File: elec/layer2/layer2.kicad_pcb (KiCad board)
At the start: 2 copper layers, 178 x 173.3 mm, 33 parts, among them J1 Conn_01x08, J2 Conn_01x08, J3 Conn_01x08, J4 Conn_01x08

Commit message: l1 half motors done
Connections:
- L1-->l2Connection1 pad 1: /Dribbler Data -> /LightGateLDR
- L1-->l2Connection1 pad 2: /LightGateLDR -> /Dribbler Data
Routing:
- net /Dribbler Data: track 108.4 -> 112.0 mm
- net /LightGateLDR: track 122.2 -> 123.5 mm
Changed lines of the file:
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@@
 			(layers "*.Cu" "*.Mask")
 			(remove_unused_layers no)
-			(net 15 "/Dribbler Data")
+			(net 2 "/LightGateLDR")
 			(pinfunction "Pin_1")
 			(pintype "passive")
@@
 			(layers "*.Cu" "*.Mask")
 			(remove_unused_layers no)
-			(net 2 "/LightGateLDR")
+			(net 15 "/Dribbler Data")
 			(pinfunction "Pin_2")
 			(pintype "passive")
@@
 	)
 	(segment
+		(start 91.407681 47.345234)
+		(end 93.607681 47.345234)
+		(width 0.2)
+		(layer "F.Cu")
+		(net 2)
+	)
+	(segment
 		(start 89.557681 144.245234)
 		(end 89.557681 157.995234)
@@
 	)
 	(segment
-		(start 88.707681 45.845234)
-		(end 89.747681 44.805234)
+		(start 91.207681 105.495234)
+		(end 91.207681 106.445234)
+		(width 0.2)
+		(layer "F.Cu")
+		(net 2)
+	)
+	(segment
+		(start 93.407681 106.845234)
+		(end 94.107681 106.145234)
 		(width 0.2)
 		(layer "F.Cu")
@@
 	)
 	(segment
-		(start 88.707681 102.545234)
-		(end 88.707681 45.845234)
+		(start 90.307681 99.745234)
+		(end 90.307681 48.445234)
 		(width 0.2)
 		(layer "F.Cu")
@@
 	)
 	(segment
-		(start 91.207681 105.045234)
-		(end 88.707681 102.545234)
+		(start 91.607681 106.845234)
+		(end 93.407681 106.845234)
 		(width 0.2)
 		(layer "F.Cu")
@@
 	)
 	(segment
-		(start 91.207681 127.745234)
-		(end 91.207681 142.595234)
+		(start 91.207681 106.445234)
+		(end 91.607681 106.845234)
 		(width 0.2)
 		(layer "F.Cu")
@@
 	)
 	(segment
-		(start 89.747681 44.805234)
-		(end 93.607681 44.805234)
+		(start 94.107681 103.545234)
+		(end 90.307681 99.745234)
 		(width 0.2)
 		(layer "F.Cu")
@@
 	)
 	(segment
-		(start 91.207681 105.495234)
-		(end 91.207681 105.045234)
+		(start 94.107681 106.145234)
+		(end 94.107681 103.545234)
+		(width 0.2)
+		(layer "F.Cu")
+		(net 2)
+	)
+	(segment
+		(start 90.307681 48.445234)
+		(end 91.407681 47.345234)
+		(width 0.2)
+		(layer "F.Cu")
+		(net 2)
+	)
+	(segment
+		(start 91.207681 127.745234)
+		(end 91.207681 142.595234)
 		(width 0.2)
 		(layer "F.Cu")
@@
 	)
 	(segment
-		(start 90.407681 101.945234)
-		(end 92.907681 104.445234)
+		(start 88.707681 47.545234)
+		(end 91.447681 44.805234)
 		(width 0.2)
 		(layer "F.Cu")
@@
 	(segment
 		(start 92.907681 104.445234)
-		(end 92.907681 105.445234)
+		(end 88.707681 100.245234)
 		(width 0.2)
 		(layer "F.Cu")
@@
 	)
 	(segment
-		(start 90.807681 47.345234)
-		(end 90.407681 47.745234)
+		(start 92.907681 105.445234)
+		(end 92.907681 104.445234)
 		(width 0.2)
 		(layer "F.Cu")
@@
 	)
 	(segment
-		(start 90.407681 47.745234)
-		(end 90.407681 101.945234)
+		(start 91.447681 44.805234)
+		(end 93.607681 44.805234)
 		(width 0.2)
 		(layer "F.Cu")
@@
 	)
 	(segment
-		(start 93.607681 47.345234)
-		(end 90.807681 47.345234)
+		(start 88.707681 100.245234)
+		(end 88.707681 47.545234)
 		(width 0.2)
 		(layer "F.Cu")

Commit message: touched lit 1 thing on l2
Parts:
- moved J1 1.60 mm to (91.6, 50.9)
- moved U3 1.60 mm to (100.4, 66.2)
- moved J2 1.60 mm to (91.5, 81.6)
- moved J3 1.60 mm to (122.4, 50.9)
- moved J4 1.60 mm to (122.3, 81.5)
- moved U3 1.60 mm to (131.2, 66.2)
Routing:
- net +24V: track 57.0 -> 45.5 mm

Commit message: l1+l2 added jsts
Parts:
- removed L2-->l2Connection2: Conn_01x09, Pinheaders:PinHeader_1x09_P2.54mm_Vertical
- added L1-->l3Connection2: Conn_01x09, Connector_JST:JST_XH_B9B-XH-AM_1x09_P2.50mm_Vertical, F.Cu at (137.6, 47.3)
- L1-->l2Connection1: footprint Pinheaders:PinHeader_1x09_P2.54mm_Vertical -> Connector_JST:JST_XH_B9B-XH-AM_1x09_P2.50mm_Vertical
- moved L1-->l2Connection1 0.50 mm to (94.1, 47.3), turned to 90 degrees
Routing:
- net +24V: track 45.5 -> 54.6 mm
- net +5V: track 68.6 -> 66.1 mm
- net +12V: track 364.5 -> 366.0 mm
- net +3V3: track 410.6 -> 410.0 mm
- net GND: vias 13 -> 20

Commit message: wdicajdfkj,
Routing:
- net +12V: track 366.0 -> 325.2 mm
- net /Sol: track 83.5 -> 91.3 mm, vias 2 -> 1
- net /LightGateLDR: track 124.0 -> 128.4 mm
- net +3V3: track 410.0 -> 410.5 mm
- net GND: vias 20 -> 21

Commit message: Revert "wdicajdfkj,"
This reverts commit e49fd520bb1bff58c9ec61a88596577cb6380b2a.
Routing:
- net +12V: track 325.2 -> 366.0 mm
- net /Sol: track 91.3 -> 83.5 mm, vias 1 -> 2
- net /LightGateLDR: track 128.4 -> 124.0 mm
- net +3V3: track 410.5 -> 410.0 mm
- net GND: vias 21 -> 20

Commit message: unfucked bucks and touched on l1/2
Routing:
- net /Sol: track 83.5 -> 93.6 mm, vias 2 -> 1
- net /LightGateLDR: track 124.0 -> 128.2 mm
- net +12V: track 366.0 -> 364.5 mm
- net +3V3: track 410.0 -> 410.9 mm

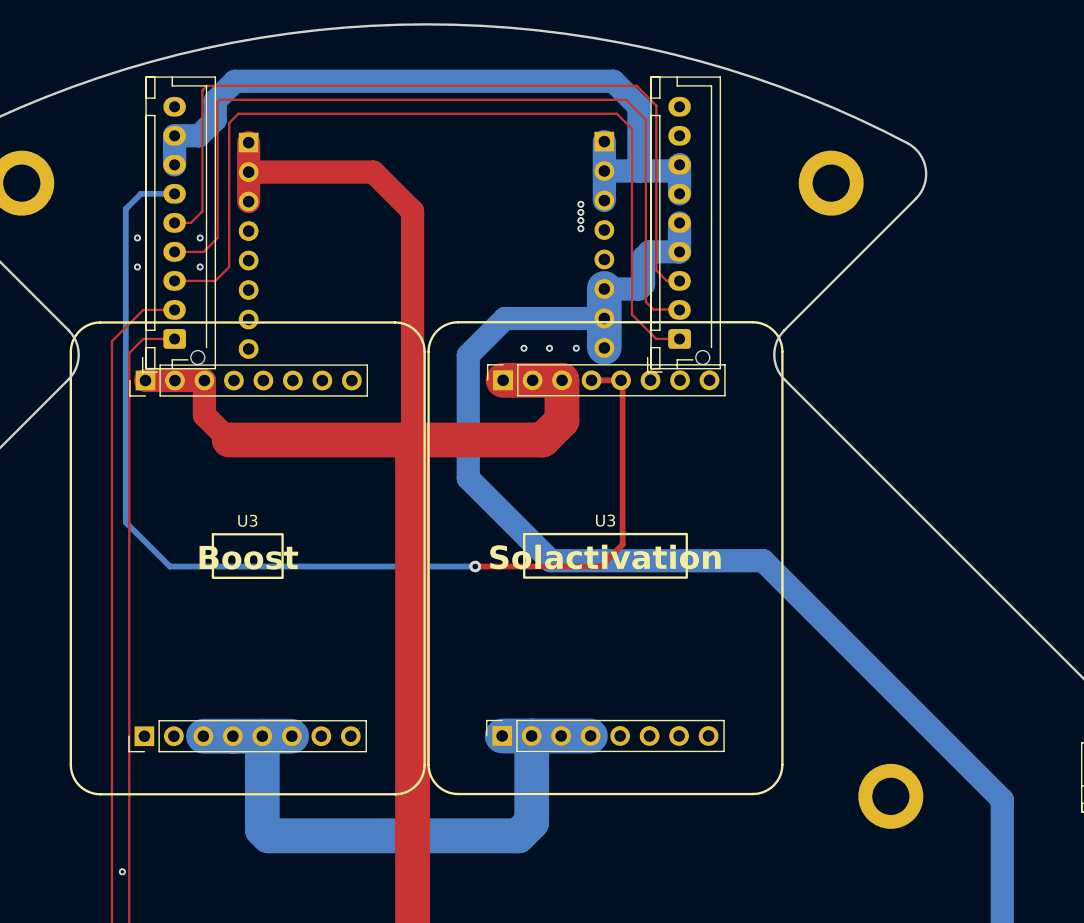
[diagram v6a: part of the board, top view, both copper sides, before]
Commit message: did pcba for tofs+increased dist between l1 to3 connection and sol activationi
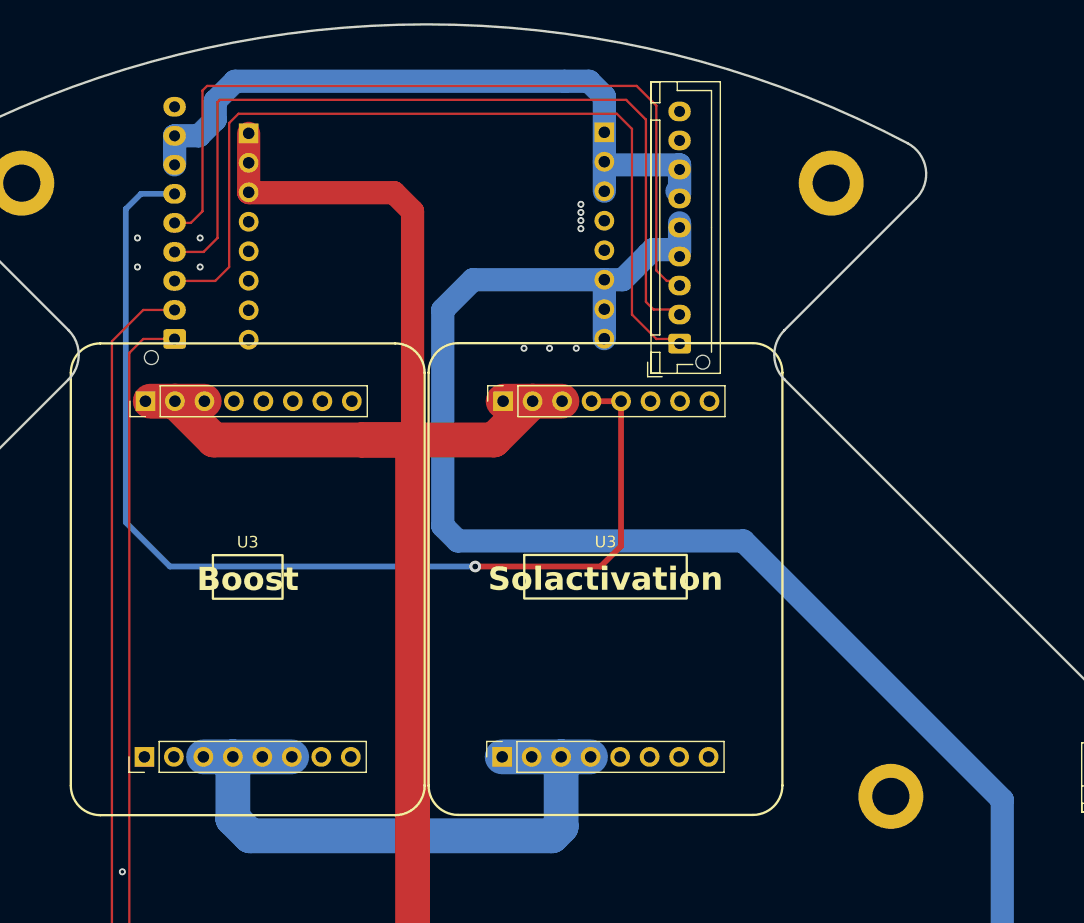
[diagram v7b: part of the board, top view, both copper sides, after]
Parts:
- L1-->l2Connection1: moved to B.Cu
- moved J4 1.80 mm to (122.3, 83.3)
- moved J3 1.80 mm to (122.4, 52.7)
- moved U3 1.80 mm to (100.4, 68.0)
- moved U3 1.80 mm to (131.2, 68.0)
- moved J2 1.78 mm to (91.5, 83.3)
- moved J1 1.78 mm to (91.6, 52.7)
- moved U1 0.80 mm to (115.8, 38.4)
- moved L1-->l3Connection2 0.40 mm to (137.6, 47.7)
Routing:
- net +3V3: track 410.9 -> 419.8 mm
- net +5V: track 66.1 -> 60.5 mm
- net +12V: track 364.5 -> 362.5 mm
- net /Sol: track 93.6 -> 91.7 mm
- net +24V: track 54.6 -> 55.8 mm

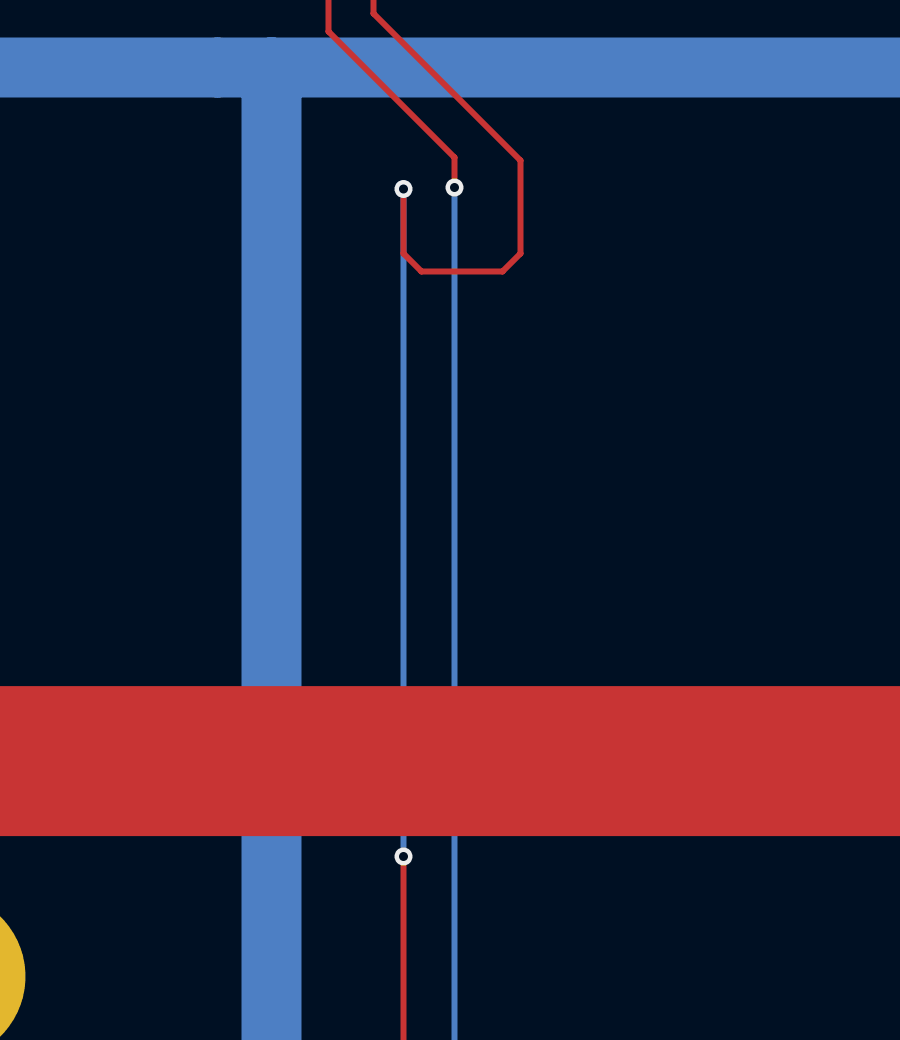
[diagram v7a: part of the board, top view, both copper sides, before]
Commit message: l2 : moved a singular via
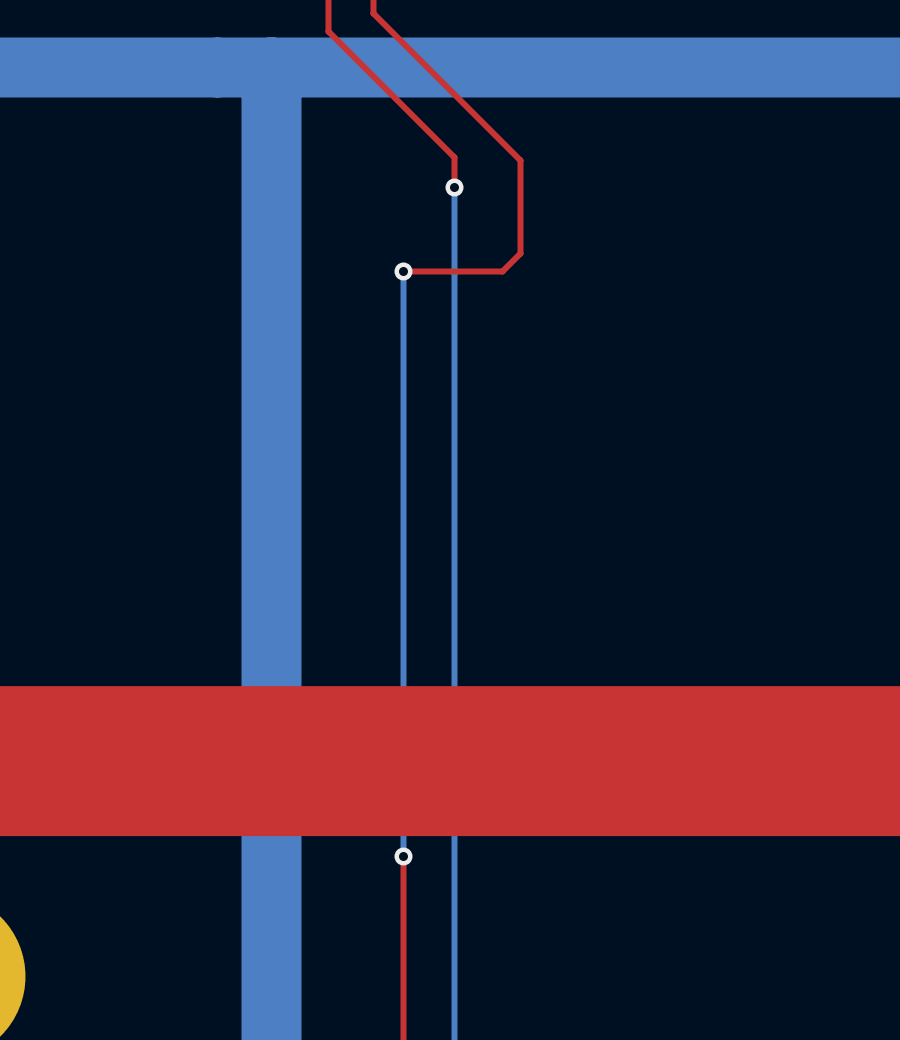
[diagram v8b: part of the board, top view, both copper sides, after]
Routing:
- net /LightGateLDR: track 128.2 -> 123.1 mm
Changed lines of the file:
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@@
 	)
 	(segment
-		(start 90.207681 99.645234)
-		(end 90.207681 48.545234)
+		(start 95.107681 107.645234)
+		(end 95.107681 104.545234)
 		(width 0.2)
 		(layer "F.Cu")
@@
 	)
 	(segment
-		(start 90.207681 48.545234)
-		(end 91.407681 47.345234)
-		(width 0.2)
-		(layer "F.Cu")
-		(net 2)
-	)
-	(segment
-		(start 88.807681 158.745234)
-		(end 86.882681 158.745234)
-		(width 0.2)
-		(layer "F.Cu")
-		(net 2)
-	)
-	(segment
-		(start 91.807681 108.245234)
+		(start 91.207681 108.245234)
 		(end 94.507681 108.245234)
 		(width 0.2)
@@
 	)
 	(segment
-		(start 91.207681 105.495234)
-		(end 91.207681 107.645234)
+		(start 88.807681 158.745234)
+		(end 86.882681 158.745234)
 		(width 0.2)
 		(layer "F.Cu")
@@
 	)
 	(segment
-		(start 94.507681 108.245234)
-		(end 95.107681 107.645234)
+		(start 90.207681 99.645234)
+		(end 90.207681 48.545234)
 		(width 0.2)
 		(layer "F.Cu")
@@
 	)
 	(segment
-		(start 95.107681 107.645234)
-		(end 95.107681 104.545234)
+		(start 90.207681 48.545234)
+		(end 91.407681 47.345234)
 		(width 0.2)
 		(layer "F.Cu")
@@
 	)
 	(segment
-		(start 91.207681 107.645234)
-		(end 91.807681 108.245234)
+		(start 91.407681 47.345234)
+		(end 94.107681 47.345234)
 		(width 0.2)
 		(layer "F.Cu")
@@
 	)
 	(segment
-		(start 91.407681 47.345234)
-		(end 94.107681 47.345234)
+		(start 94.507681 108.245234)
+		(end 95.107681 107.645234)
 		(width 0.2)
 		(layer "F.Cu")
@@
 	)
 	(via
-		(at 91.207681 105.495234)
+		(at 91.207681 108.245234)
 		(size 0.6)
 		(drill 0.3)
@@
 	(segment
 		(start 91.207681 127.745234)
-		(end 91.207681 105.495234)
+		(end 91.207681 108.245234)
 		(width 0.2)
 		(layer "B.Cu")
